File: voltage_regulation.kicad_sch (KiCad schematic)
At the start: 30 parts, among them IC3 TPS5430DDAR, U1 TPS73601MDBVREP, U2 TPS73601MDBVREP

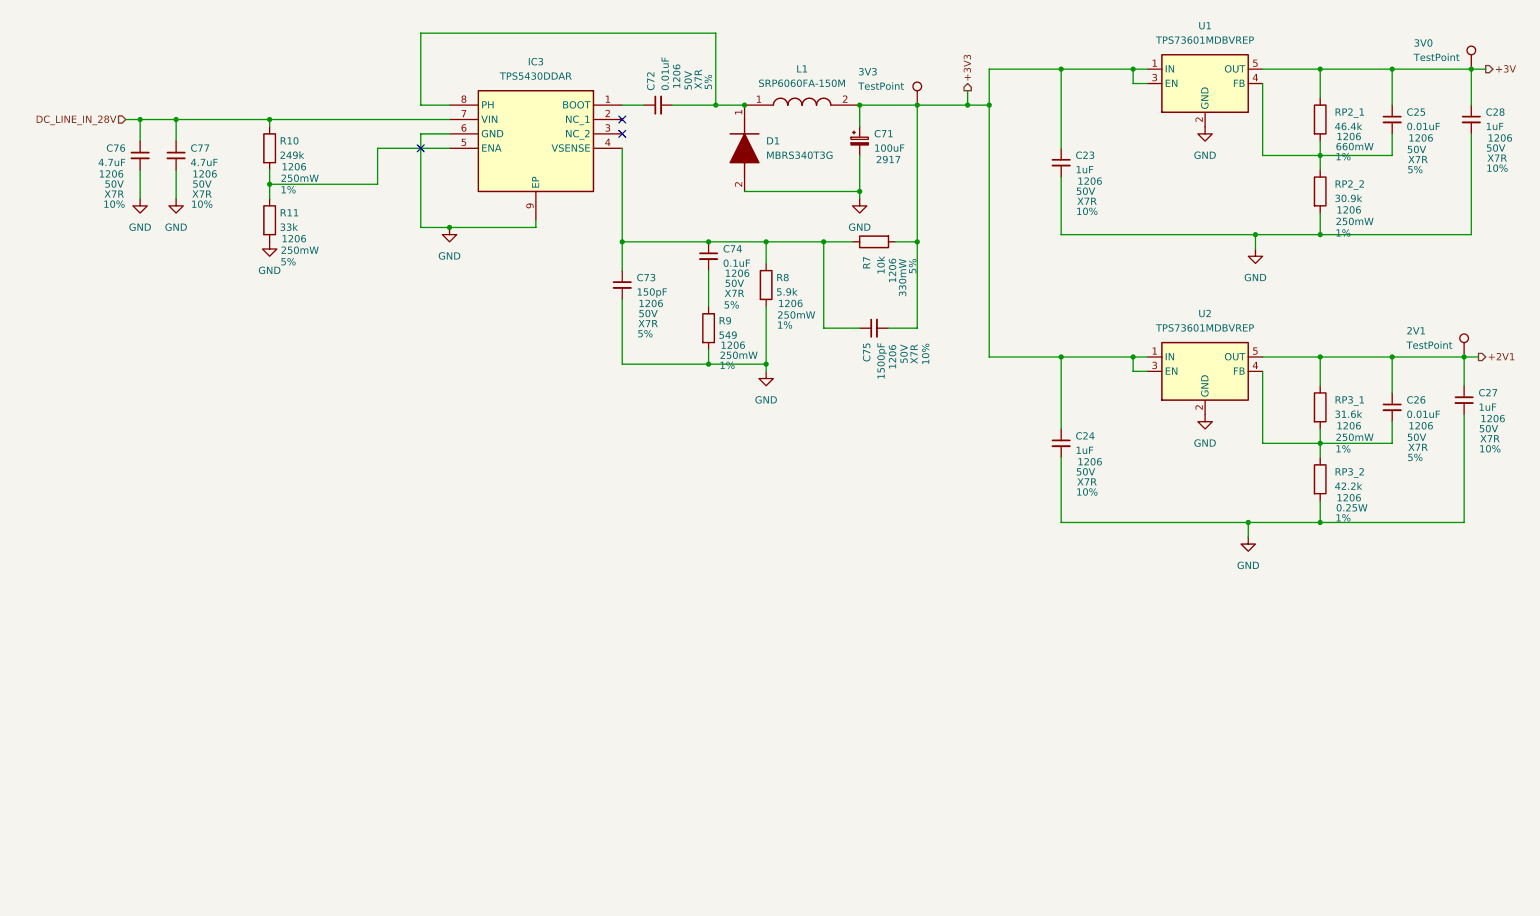
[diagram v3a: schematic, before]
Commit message: V3 Overhaul
Things remaining:
Ethernet Transceiver Clocks
Output Filtering on DC-DC Converter
Update some part numbers
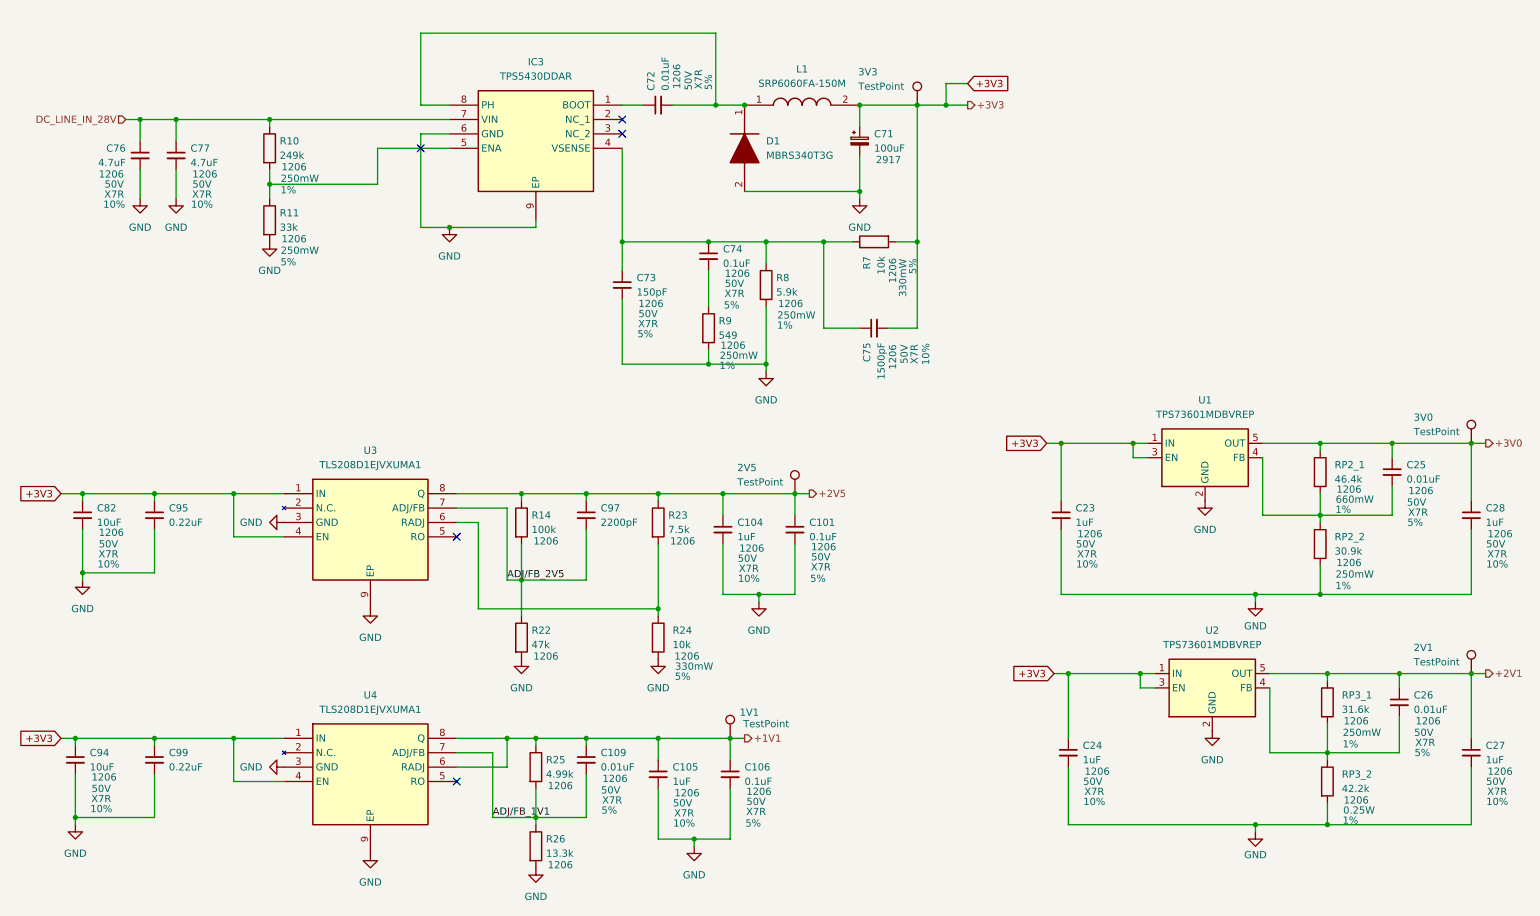
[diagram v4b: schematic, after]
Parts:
- added 1V1, 2V5: TestPoint, TestPoint:TestPoint_Pad_D1.0mm, symbol Connector:TestPoint
- added C101, C106: 0.1uF, Capacitor_SMD:C_1206_3216Metric, symbol Device:C_Small
- added C104, C105: 1uF, Capacitor_SMD:C_1206_3216Metric, symbol Device:C_Small
- added C109: 0.01uF, Capacitor_SMD:C_1206_3216Metric, symbol Device:C_Small
- added C82, C94: 10uF, Capacitor_SMD:C_1206_3216Metric, symbol Device:C_Small
- added C95, C99: 0.22uF, Capacitor_SMD:C_1206_3216Metric, symbol Device:C_Small
- added C97: 2200pF, Capacitor_SMD:C_1206_3216Metric, symbol Device:C_Small
- added R14: 100k, Resistor_SMD:R_1206_3216Metric, symbol Device:R
- added R22: 47k, Resistor_SMD:R_1206_3216Metric, symbol Device:R
- added R23: 7.5k, Resistor_SMD:R_1206_3216Metric, symbol Device:R
- added R24: 10k, Resistor_SMD:R_1206_3216Metric, symbol Device:R
- added R25: 4.99k, Resistor_SMD:R_1206_3216Metric, symbol Device:R
- added R26: 13.3k, Resistor_SMD:R_1206_3216Metric, symbol Device:R
- added U3, U4: TLS208D1EJVXUMA1, SOIC127P600X170-9N, symbol SamacSys_Parts:TLS208D1EJVXUMA1
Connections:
- net +3V3: now also C82.1, C94.1, C95.1, C99.1, U3.1 (IN), U3.4 (EN), U4.1 (IN), U4.4 (EN)
- net GND: now also C101.2, C104.2, C105.2, C106.2, C82.2, C94.2, C95.2, C99.2, R22.2, R24.2, R26.2, U3.3 (GND), U3.9 (EP), U4.3 (GND), U4.9 (EP)
- net +3V renamed +3V0
- new net: R23.2, R24.1, U3.6 (RADJ)
- new net +1V1: 1V1.1, C105.1, C106.1, C109.1, R25.1, U4.6 (RADJ), U4.8 (Q)
- new net +2V5: 2V5.1, C101.1, C104.1, C97.1, R14.1, R23.1, U3.8 (Q)
- new net ADJ/FB_1V1: C109.2, R25.2, R26.1, U4.7 (ADJ/FB)
- new net ADJ/FB_2V5: C97.2, R14.2, R22.1, U3.7 (ADJ/FB)
- no-connect marks 3 -> 5
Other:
- moved on the sheet: 2V1, 3V0, C23, C24, C25, C26, C27, C28, RP2_1, RP2_2, RP3_1, RP3_2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

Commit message: Keepouts on mounting holes, QSPI on different lines, new LVDS clock buffer, voltage sense circuit
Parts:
- U3, U4: footprint SOIC127P600X170-9N -> SamacSys_Parts:SOIC127P600X170-9N
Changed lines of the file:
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@@
 			)
 		)
-		(property "Footprint" "SOIC127P600X170-9N"
+		(property "Footprint" "SamacSys_Parts:SOIC127P600X170-9N"
 			(at 88.9 195.25 0)
 			(effects
@@
 			)
 		)
-		(property "Footprint" "SOIC127P600X170-9N"
+		(property "Footprint" "SamacSys_Parts:SOIC127P600X170-9N"
 			(at 88.9 238.43 0)
 			(effects
